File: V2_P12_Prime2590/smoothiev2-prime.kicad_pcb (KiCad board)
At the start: 4 copper layers, 110 x 110 mm, 453 parts, among them J1 USB_B, J10 Conn_01x02, J11 Conn_01x02, J12 Conn_01x02, J13 Conn_01x02, J14 Conn_01x02, J15 Conn_01x02, J16 Conn_01x02, J17 Conn_01x02, J18 Conn_01x02, J19 Conn_01x02, J2 USB_A, J20 Conn_01x02, J21 Conn_01x02, J22 Conn_01x02, J23 Conn_01x02, J24 Conn_01x03, J25 Conn_01x03, J26 Conn_01x03, J27 Conn_01x03, J28 Conn_01x03, J29 Conn_01x03, J3 Micro_SD_Card_Det, J30 Conn_01x03_Male, J31 Conn_01x04, J32 Conn_02x05_Odd_Even, J33 Conn_02x05_Odd_Even, J34 Conn_02x05_Odd_Even, J35 Conn_02x05_Odd_Even, J36 Conn_02x05_Odd_Even, J37 Conn_02x05_Odd_Even, J38 Conn_02x05_Odd_Even, J39 Conn_02x05_Odd_Even, J4 RJ45_Hanrun_HR911105A, J40 Conn_02x05_Odd_Even, J41 Conn_ARM_JTAG_SWD_10, J42 Conn_01x02, J43 Conn_01x02, J44 Conn_01x02, J45 Conn_01x02, J5 Screw_Terminal_01x04, J6 Screw_Terminal_01x04, J7 Screw_Terminal_01x04, J8 Screw_Terminal_01x04, J9 Conn_01x02, Q1 Si4542DY, Q10 Si4542DY, Q11 Si4542DY, Q12 Si4542DY, Q13 Si4542DY, Q14 Si4542DY, Q15 Si4542DY, Q16 Si4542DY, Q17 WSD3066DN33, Q18 WSD3066DN33, Q19 WSD3066DN33, Q2 Si4542DY, Q20 WSD3066DN33, Q21 WSD3066DN33, Q22 WSD3066DN33, Q23 CJ2301 S1, Q24 CJ2301 S1, Q25 WSD30L40DN, Q26 2N7002, Q27 MBT3906DW1, Q28 SQ3493EV, Q29 MBT3906DW1, Q3 Si4542DY, Q30 SQ3493EV, Q31 MBT3906DW1, Q32 SQ3493EV, Q4 Si4542DY, Q5 Si4542DY, Q6 Si4542DY, Q7 Si4542DY, Q8 Si4542DY, Q9 Si4542DY, SW1 SW_Push, SW2 TS-1185EC-C-D-B, U1 LAN8720A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

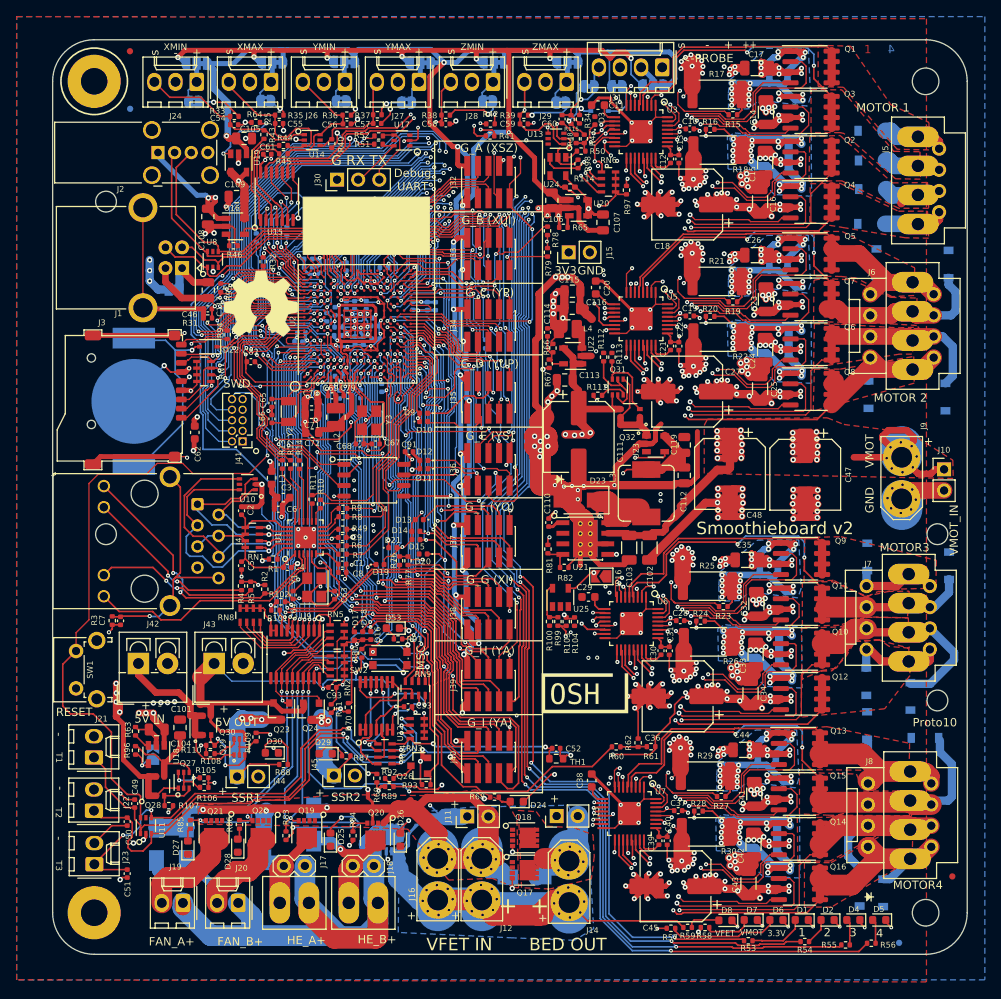
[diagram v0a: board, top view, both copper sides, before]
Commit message: Convert both projects to V8 format fix DRC and ERC (except silkscreen) space out the VFET connectors slightly
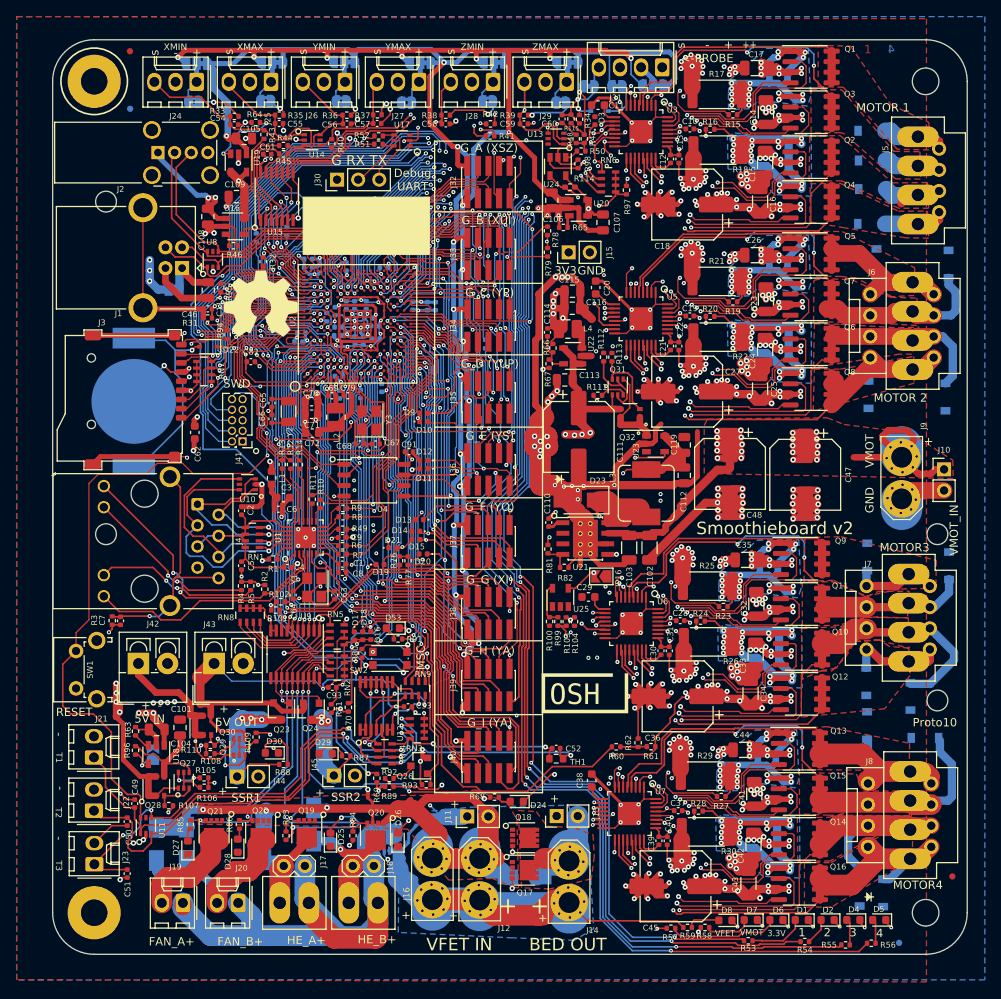
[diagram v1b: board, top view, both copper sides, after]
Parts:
- NT1, NT2, NT3, NT4, NT5, NT6, NT7, NT8: footprint smoothieparts:NetTie-2_SMD_Pad2.0mm -> Library:NetTie-2_SMD_Pad2.0mm
- moved J16 0.65 mm to (145.5, 138.9)
- moved D26 0.28 mm to (141.4, 134.2)
- moved Q25 0.26 mm to (140.7, 134.1)
- moved J12 0.25 mm to (151.2, 139.0)
- moved R115 0.08 mm to (162.2, 47.5)
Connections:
- J41 pad 7: Net-(J41-Pad7) -> unconnected-(J41-KEY-Pad7)
- U10 pad 5: Net-(U10-Pad5) -> unconnected-(U10-Pad5)
- U11 pad 5: Net-(U11-Pad5) -> unconnected-(U11-Pad5)
- U13 pad 3: Net-(U13-Pad3) -> unconnected-(U13-Pad3)
- U13 pad 5: Net-(U13-Pad5) -> unconnected-(U13-Pad5)
- U13 pad 6: Net-(U13-Pad6) -> unconnected-(U13-Pad6)
- U14 pad 5: Net-(U14-Pad5) -> unconnected-(U14-Pad5)
- U17 pad 1: Net-(U17-Pad1) -> unconnected-(U17-Pad1)
- U17 pad 3: Net-(U17-Pad3) -> unconnected-(U17-Pad3)
- U17 pad 5: Net-(U17-Pad5) -> unconnected-(U17-Pad5)
- U2 pad B7: Net-(U2-PadB7) -> unconnected-(U2-PB4-PadB7)
- U2 pad C7: Net-(U2-PadC7) -> unconnected-(U2-PK6-PadC7)
- U2 pad C8: Net-(U2-PadC8) -> unconnected-(U2-PK3-PadC8)
- U2 pad D11: Net-(U2-PadD11) -> unconnected-(U2-PJ12-PadD11)
- U2 pad D14: Net-(U2-PadD14) -> unconnected-(U2-PA10-PadD14)
- U2 pad D6: Net-(U2-PadD6) -> unconnected-(U2-PG15-PadD6)
- U2 pad D7: Net-(U2-PadD7) -> unconnected-(U2-PK7-PadD7)
- U2 pad D8: Net-(U2-PadD8) -> unconnected-(U2-PG14-PadD8)
- U2 pad E12: Net-(U2-PadE12) -> unconnected-(U2-PD1-PadE12)
- U2 pad F13: Net-(U2-PadF13) -> unconnected-(U2-PC7-PadF13)
- U2 pad H1: Net-(U2-PadH1) -> unconnected-(U2-PI12-PadH1)
- U2 pad H2: Net-(U2-PadH2) -> unconnected-(U2-PI13-PadH2)
- U2 pad H3: Net-(U2-PadH3) -> unconnected-(U2-PI14-PadH3)
- U2 pad H4: Net-(U2-PadH4) -> unconnected-(U2-PF3-PadH4)
- U2 pad J4: Net-(U2-PadJ4) -> unconnected-(U2-PF5-PadJ4)
- U2 pad K16: Net-(U2-PadK16) -> unconnected-(U2-NC-PadK16)
- U2 pad K17: Net-(U2-PadK17) -> unconnected-(U2-NC-PadK17)
- U2 pad K3: Net-(U2-PadK3) -> unconnected-(U2-PF7-PadK3)
- U2 pad L16: Net-(U2-PadL16) -> unconnected-(U2-NC-PadL16)
- U2 pad L17: Net-(U2-PadL17) -> unconnected-(U2-NC-PadL17)
- U2 pad M16: Net-(U2-PadM16) -> unconnected-(U2-NC-PadM16)
- U2 pad M17: Net-(U2-PadM17) -> unconnected-(U2-NC-PadM17)
- U2 pad N17: Net-(U2-PadN17) -> unconnected-(U2-NC-PadN17)
- U2 pad N5: Net-(U2-PadN5) -> unconnected-(U2-PA0-PadN5)
- U2 pad N6: Net-(U2-PadN6) -> unconnected-(U2-PJ0-PadN6)
- U2 pad N9: Net-(U2-PadN9) -> unconnected-(U2-PE10-PadN9)
- U2 pad P5: Net-(U2-PadP5) -> unconnected-(U2-PI15-PadP5)
- U2 pad P6: Net-(U2-PadP6) -> unconnected-(U2-PJ1-PadP6)
- U2 pad R1: Net-(U2-PadR1) -> unconnected-(U2-PC2_C-PadR1)
- U2 pad R11: Net-(U2-PadR11) -> unconnected-(U2-PE15-PadR11)
- U2 pad R12: Net-(U2-PadR12) -> unconnected-(U2-PJ5-PadR12)
- U2 pad R2: Net-(U2-PadR2) -> unconnected-(U2-PC3_C-PadR2)
- U2 pad T11: Net-(U2-PadT11) -> unconnected-(U2-PH6-PadT11)
- U2 pad T2: Net-(U2-PadT2) -> unconnected-(U2-PA1_C-PadT2)
- U21 pad 2: Net-(U21-Pad2) -> unconnected-(U21-NC-Pad2)
- U21 pad 3: Net-(U21-Pad3) -> unconnected-(U21-NC-Pad3)
- U23 pad 3: Net-(U23-Pad3) -> unconnected-(U23-~{FLG}-Pad3)
- U8 pad 5: Net-(U8-Pad5) -> unconnected-(U8-Pad5)
- U9 pad 11: Net-(U9-Pad11) -> unconnected-(U9-Y7-Pad11)
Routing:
- net /VMOT: track 490.6 -> 487.6 mm
- net Net-(JP18-Pad2): track 7.52 -> 8.62 mm
- net /power/UVLO: track 35.3 -> 34.6 mm
- net /3V3_LIMIT: track 188.7 -> 188.1 mm
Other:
- net class Default removed
- net class HighCurrent removed
- net class Power removed
- net class Signal removed
